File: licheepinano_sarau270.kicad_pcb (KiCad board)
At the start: 2 copper layers, 81.3 x 51.9 mm, 111 parts, among them Con1 SIM8050-6-0-14-01-A, Con2 >VALUE, Con3 USB_C_Wurth_632723130112, P1 RF2-03E-T-00-50-G, Q1 BC847B, Q2 BC847B, T1 FDN304P, U1 LAN9514I, U2 IP4220CZ6, U3 LILY-W132, U4 MAX-M8C, U5 TXB0104, X1 ABM3-25.000MHZ-D2Y-T

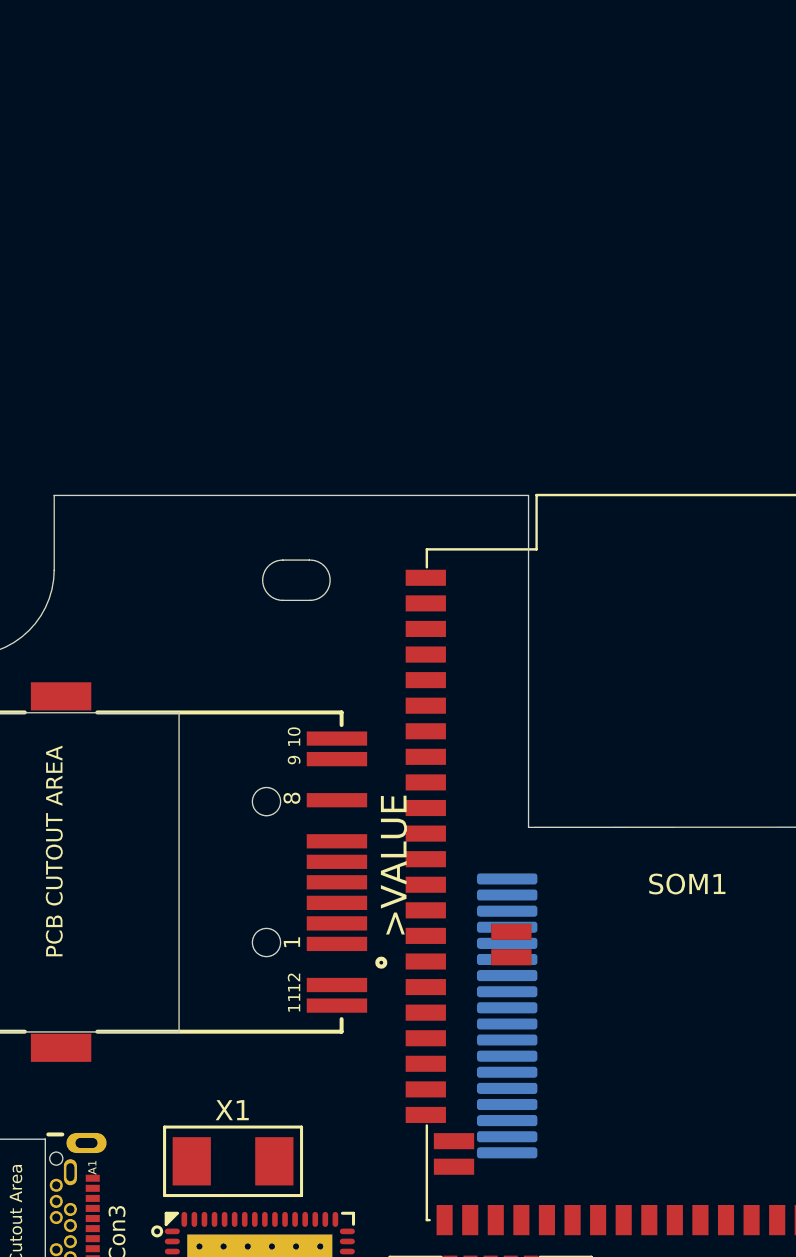
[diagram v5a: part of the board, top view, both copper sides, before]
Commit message: Schematic finished, with check ERC
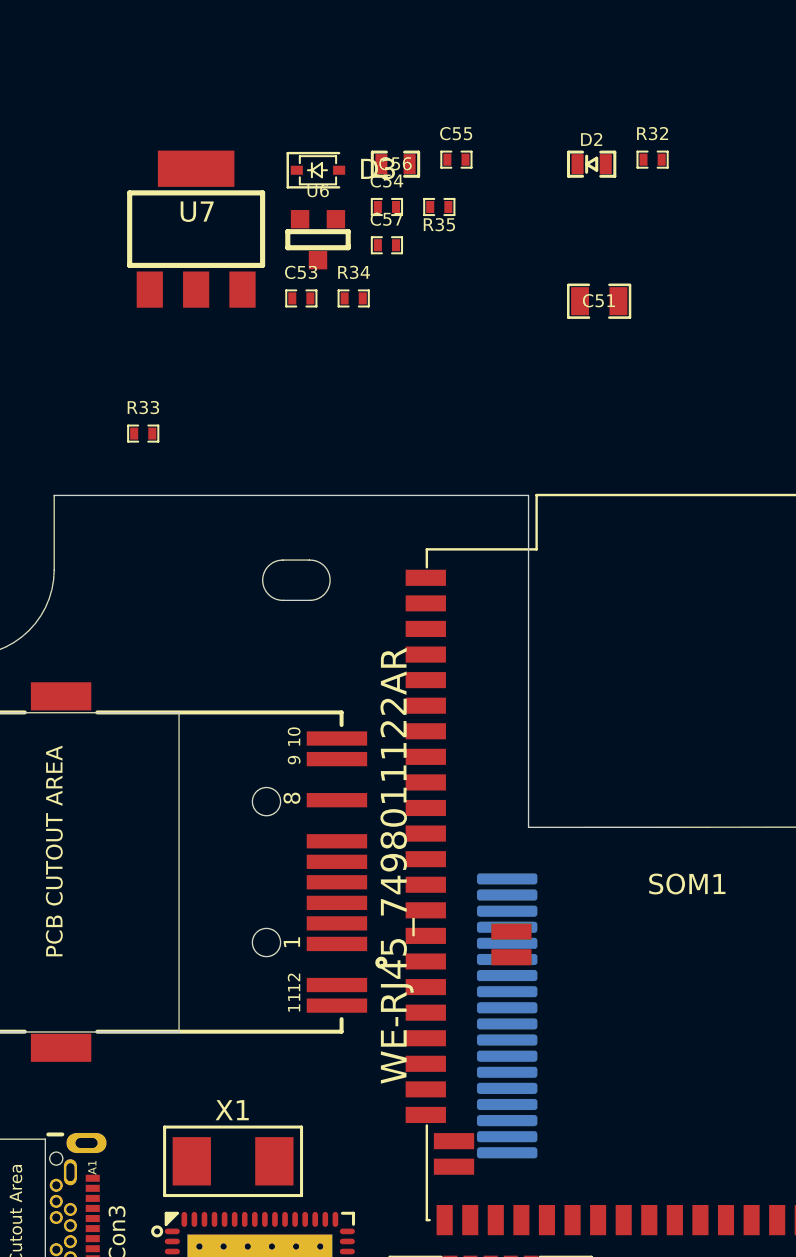
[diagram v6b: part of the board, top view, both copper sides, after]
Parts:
- added C51: 10uF/16V, Capacitors_Smd_0805:10uF_0805, F.Cu at (134.1, 62.8)
- added C53: 1uF/10V, Capacitors_Smd_0402:1uF_0402, F.Cu at (119.3, 62.7)
- added C54: 1uF/10V, Capacitors_Smd_0402:1uF_0402, F.Cu at (123.5, 58.1)
- added C55: 1uF/10V, Capacitors_Smd_0402:1uF_0402, F.Cu at (127.0, 55.8)
- added C56: 10uF/10V, Capacitors_Smd_0603:10uF_10V_0603, F.Cu at (123.9, 56.0)
- added C57: 1uF/10V, Capacitors_Smd_0402:1uF_0402, F.Cu at (123.5, 60.0)
- added D2: KPG-1608SURKC-T, Diodes:LED_KPG-1608SURKC-T, F.Cu at (133.7, 56.0)
- added D3: NSR0530H-D, Diodes:NSR0530H-D_SOD323, F.Cu at (120.1, 56.3)
- added R32: 470R, Resistor_Smd_0402:470R_0402, F.Cu at (136.7, 55.8)
- added R33: 47k, Resistor_Smd_0402:47k_0402, F.Cu at (111.4, 69.4)
- added R34: 1k5, Resistor_Smd_0402:1k5_0402, F.Cu at (121.9, 62.7)
- added R35: 3k3, Resistor_Smd_0402:3k3_0402, F.Cu at (126.1, 58.1)
- added U6: AP2127K-2.8TRG1, Linear:AP2127K-2.8TRG1_SOT23, F.Cu at (120.1, 59.8)
- added U7: LM317DCYR, Linear:LM317DCYR_SOT223, F.Cu at (114.0, 59.2)
- Con2: value >VALUE -> WE-RJ45_7498011122AR
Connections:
- net 3V8 renamed /Modem 3G/MODEM_POWER_IN
- C14 pad 1: /USB Hub Module/~HUB_RESET -> /LicheePi Nano SOM/GPIO_PD11
- C28 pad 1: /Modem 3G/LOCAL_MODEM_1V8_~RESET -> /LicheePi Nano SOM/GPIO_PD1
- C39 pad 1: /Logic Voltage Shifter/POWER_IN_HIGH_SIDE -> 3V3
- C40 pad 1: /Logic Voltage Shifter/POWER_IN_HIGH_SIDE -> 3V3
- C41 pad 1: /Logic Voltage Shifter/POWER_IN_LOW_SIDE -> /GPS Module/POWER_IN_1V8
- C42 pad 1: /Logic Voltage Shifter/POWER_IN_LOW_SIDE -> /GPS Module/POWER_IN_1V8
- Con3 pad A5: /Power Supply Module/USB_ID -> /LicheePi Nano SOM/USB_ID
- Con3 pad B5: /Power Supply Module/USB_ID -> /LicheePi Nano SOM/USB_ID
- DIS1 pad 1: /LCD Module/POWER_IN_GND -> GND
- DIS1 pad 2: (no net) -> /LicheePi Nano SOM/GPIO_PD19
- DIS1 pad 4: (no net) -> /LCD Module/DC
- DIS1 pad 8: /LCD Module/POWER_IN_GND -> GND
- DIS1 pad 9: (no net) -> /LCD Module/POWER_IN_2V8
- Modem1 pad 15: /Modem 3G/MODEM_PWR_ON -> /LicheePi Nano SOM/GPIO_PD0
- Modem1 pad 18: /Modem 3G/LOCAL_MODEM_1V8_~RESET -> /LicheePi Nano SOM/GPIO_PD1
- R13 pad 2: /Modem 3G/MODEM_PWR_ON -> /LicheePi Nano SOM/GPIO_PD0
- SOM1 pad 1: /LCD Module/MISO -> (no net)
- SOM1 pad 10: /Logic Voltage Shifter/SIG1_HIGH_PART -> /LCD Module/CS
- SOM1 pad 11: /Logic Voltage Shifter/SIG3_HIGH_PART -> (no net)
- SOM1 pad 12: /Logic Voltage Shifter/SIG2_HIGH_PART -> /LCD Module/MISO
- SOM1 pad 14: (no net) -> /LCD Module/CLK
- SOM1 pad 15: /Logic Voltage Shifter/SIG4_HIGH_PART -> (no net)
- SOM1 pad 16: (no net) -> /LCD Module/MOSI
- SOM1 pad 21: (no net) -> /LicheePi Nano SOM/GPIO_PD19
- SOM1 pad 22: (no net) -> Net-(D2-Pad2)
- SOM1 pad 25: (no net) -> /LicheePi Nano SOM/GPIO_PD5
- SOM1 pad 26: (no net) -> /Logic Voltage Shifter/SIG3_HIGH_PART
- SOM1 pad 27: (no net) -> /Logic Voltage Shifter/SIG4_HIGH_PART
- SOM1 pad 29: (no net) -> /LicheePi Nano SOM/GPIO_PD1
- SOM1 pad 3: /LCD Module/MOSI -> (no net)
- SOM1 pad 30: (no net) -> /LicheePi Nano SOM/GPIO_PD0
- SOM1 pad 31: (no net) -> /LicheePi Nano SOM/GPIO_PD11
- SOM1 pad 32: (no net) -> /UBlox WiFi Lily W132/ENABLE
- SOM1 pad 33: (no net) -> /LicheePi Nano SOM/GPIO_PD9
- SOM1 pad 34: (no net) -> /LCD Module/DC
- SOM1 pad 40: (no net) -> /Logic Voltage Shifter/SIG2_HIGH_PART
- SOM1 pad 41: (no net) -> /Logic Voltage Shifter/SIG1_HIGH_PART
- SOM1 pad 5: /LCD Module/CS -> (no net)
- SOM1 pad 63: (no net) -> /LicheePi Nano SOM/USB_ID
- SOM1 pad 7: /LCD Module/CLK -> (no net)
- U1 pad 12: /USB Hub Module/~HUB_RESET -> /LicheePi Nano SOM/GPIO_PD11
- U3 pad 14: (no net) -> /UBlox WiFi Lily W132/ENABLE
- U4 pad 9: (no net) -> /LicheePi Nano SOM/GPIO_PD9
- U5 pad 1: /Logic Voltage Shifter/POWER_IN_HIGH_SIDE -> 3V3
- U5 pad 14: /Logic Voltage Shifter/POWER_IN_LOW_SIDE -> /GPS Module/POWER_IN_1V8
- U5 pad 8: (no net) -> /LicheePi Nano SOM/GPIO_PD5

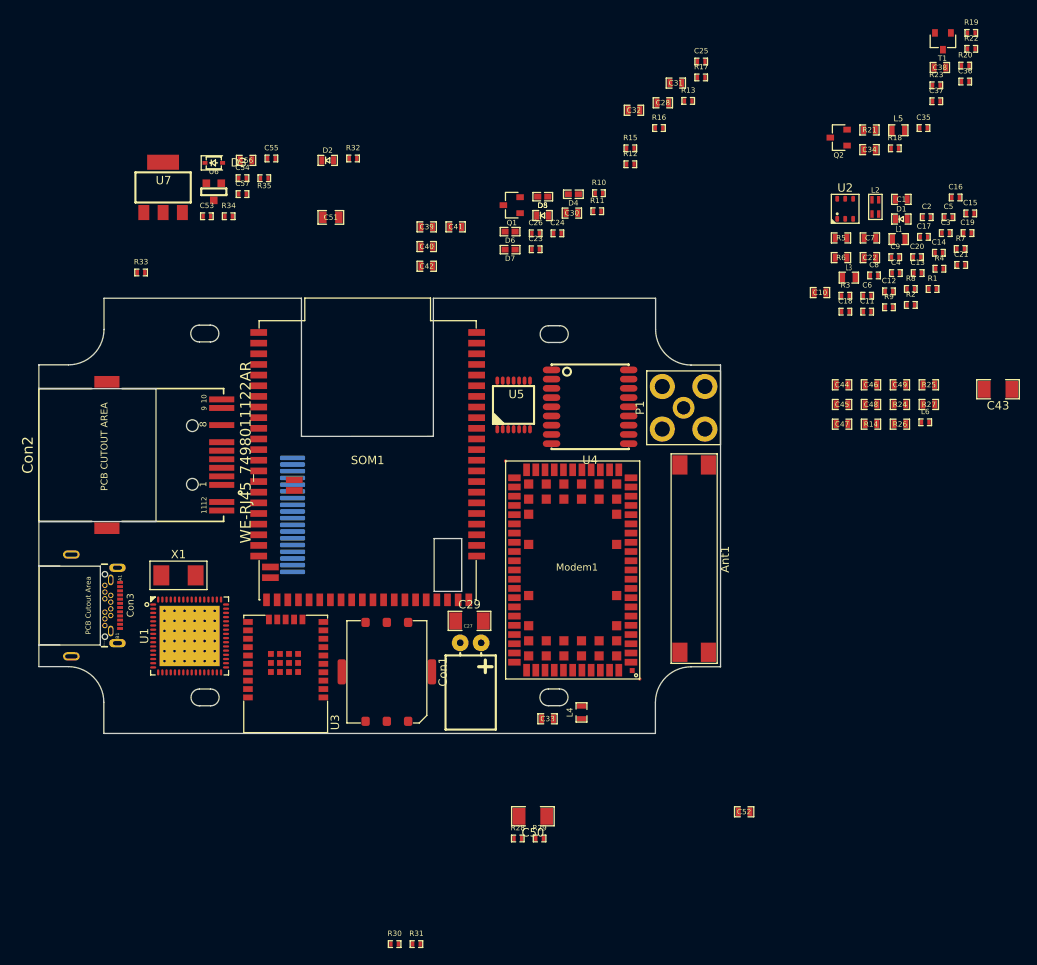
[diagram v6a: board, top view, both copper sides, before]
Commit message: Updated README.md and figurated components on pcb
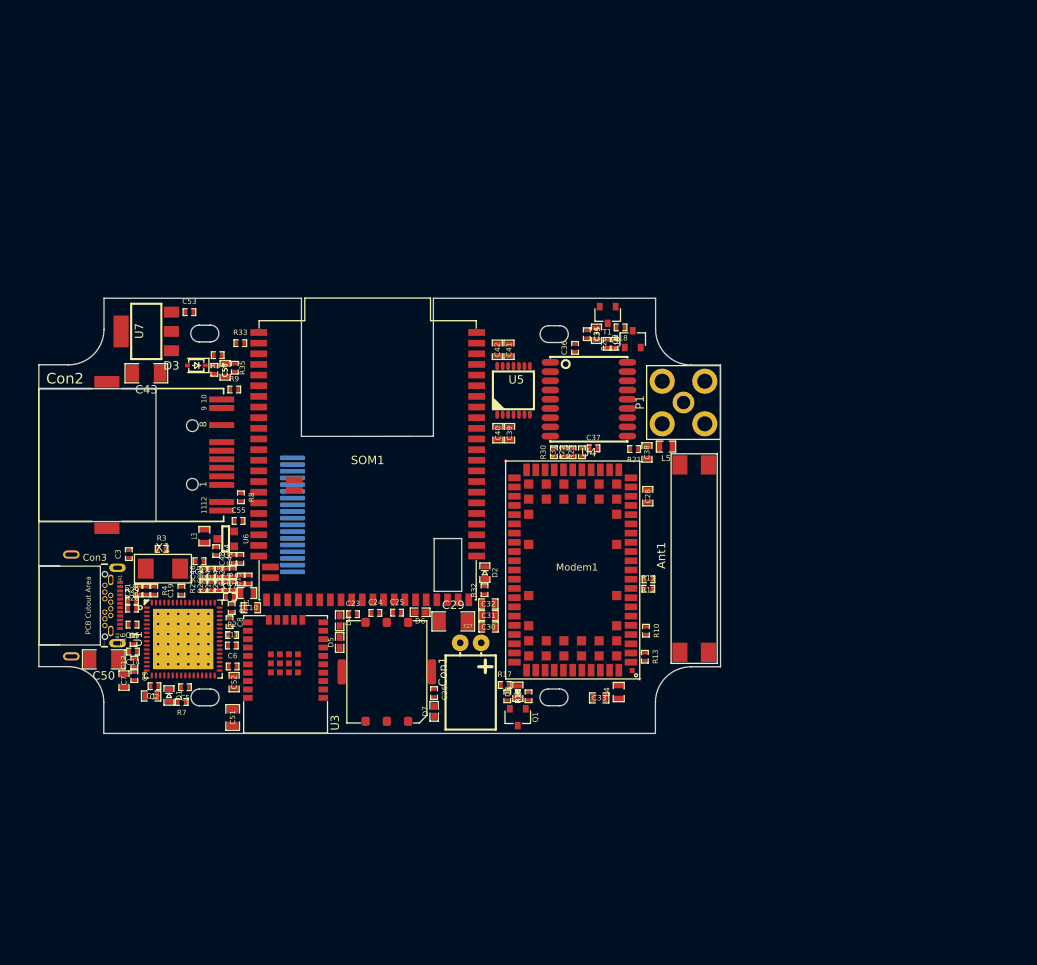
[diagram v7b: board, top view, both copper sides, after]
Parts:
- removed C22: 100nF/50V, Capacitors_Smd_0603:100nF_0603
- removed L2: DLW21HN900SQ2L, Inductors:DLW21HN900SQ2L
- removed R5, R6: 0R, Resistor_Smd_0603:0R_0603
- removed U2: IP4220CZ6, ESD_Protectors:IP4220CZ6_SOT457
- C44, C45, C46, C47: footprint Capacitors_Smd_0603:15pF_0603 -> Capacitors_Smd_0402:15pF_0402
- C48, C49: value 22nF/50V -> 22nF/25V; footprint Capacitors_Smd_0603:22nF_0603 -> Capacitors_Smd_0402:22nF_0402
- Con2: value WE-RJ45_7498011122AR -> >VALUE
- R14, R24, R25, R26: value 49R9 -> 49R9/1%; footprint Resistor_Smd_0603:49R9_0603 -> Resistor_Smd_0402:49R9_0402
- R21, R27: value 10R/1% -> 10R; footprint Resistor_Smd_0603:10R_0603 -> Resistor_Smd_0402:10R_0402
- moved C16 111.4 mm to (110.5, 113.2), turned to 90 degrees
- moved C15 111.3 mm to (110.4, 111.4), turned to 180 degrees
- moved C2 107.8 mm to (113.0, 118.7), turned to 180 degrees
- moved R7 107.5 mm to (116.3, 120.6), turned to 180 degrees
- moved C1 107.3 mm to (112.6, 119.9), turned to 180 degrees
- moved C14 107.3 mm to (110.5, 114.6), turned to 180 degrees
- moved C5 107.0 mm to (116.7, 118.8), turned to 180 degrees
- moved C21 105.6 mm to (111.1, 107.3), turned to 90 degrees
- moved C3 104.7 mm to (110.0, 103.0), turned to 90 degrees
- moved D1 104.2 mm to (114.8, 119.8), turned to 270 degrees
- moved C9 103.6 mm to (110.6, 117.5), turned to 270 degrees
- moved C7 103.5 mm to (109.4, 118.1), turned to 270 degrees
- moved C19 103.0 mm to (116.2, 107.3), turned to 90 degrees
- moved C43 101.6 mm to (112.0, 81.4)
- moved R4 101.2 mm to (113.0, 107.3), turned to 270 degrees
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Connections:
- C49 pad 1: GND -> Net-(C48-Pad1)
- C49 pad 2: Net-(C48-Pad1) -> GND
- L1 pad 2: (no net) -> Net-(C10-Pad1)
- Modem1 pad 17: VBUS -> (no net)
- U1 pad 1: /USB Hub Module/USB_HUB_5- -> /USB Hub Module/USB_D2_OUT_N
- U1 pad 2: /USB Hub Module/USB_HUB_5+ -> /USB Hub Module/USB_D2_OUT_P

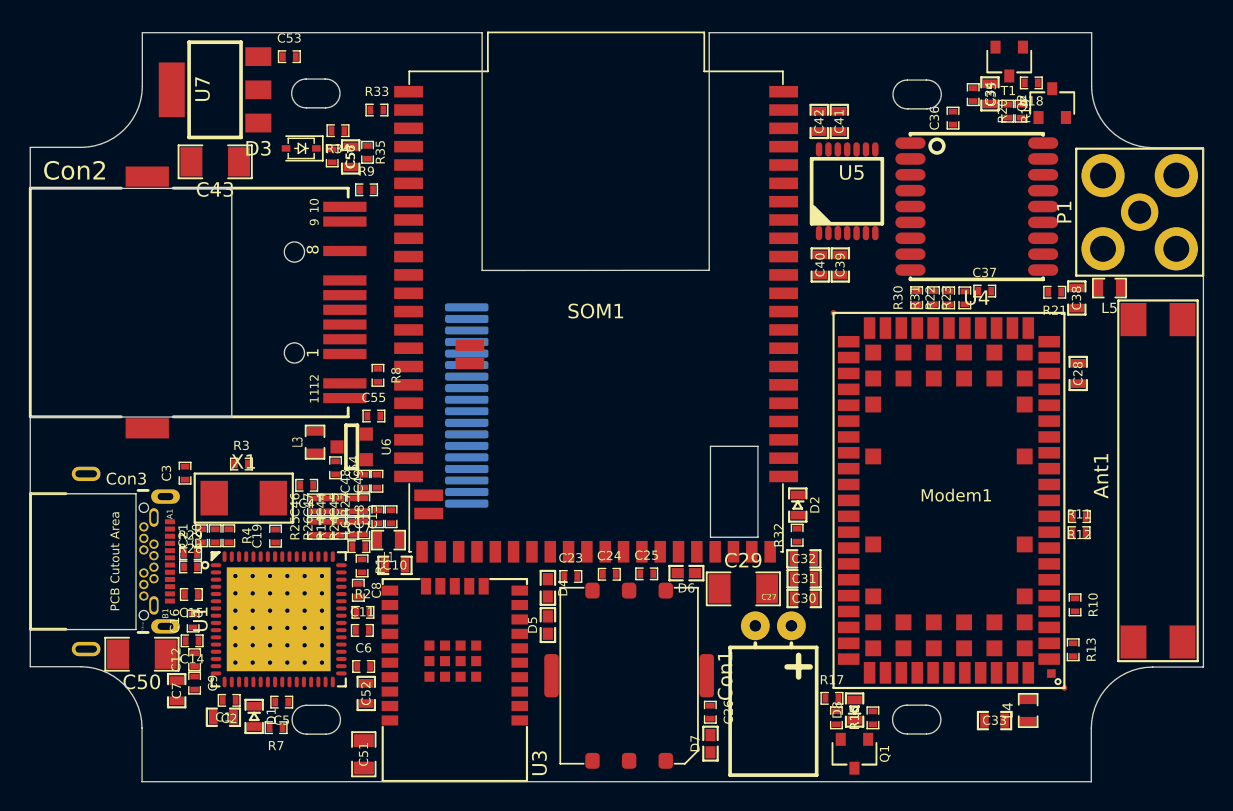
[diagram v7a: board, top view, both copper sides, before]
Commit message: Added most of the pcb connections
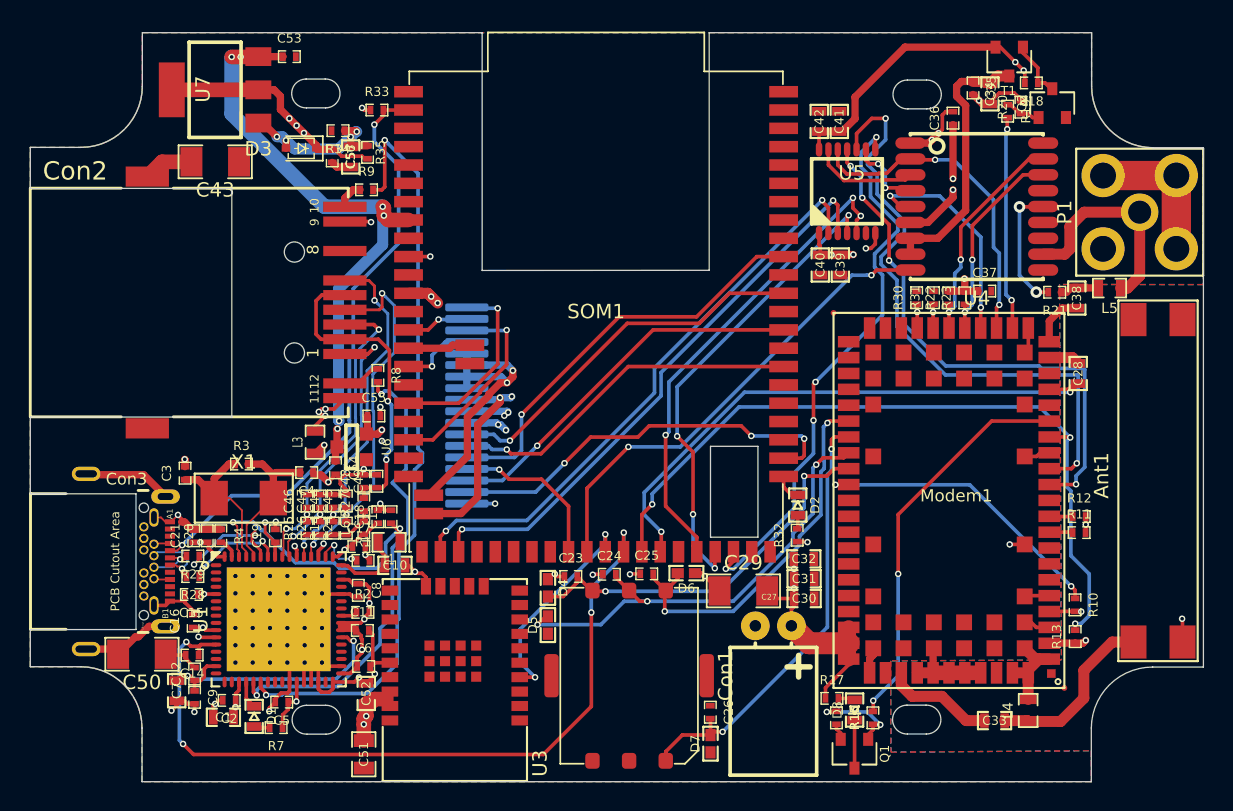
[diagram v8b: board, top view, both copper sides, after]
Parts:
- moved C12 0.99 mm to (110.6, 116.9)
- moved C14 0.99 mm to (110.5, 115.6)
- moved C9 0.99 mm to (110.6, 118.5)
- moved R13 0.92 mm to (171.7, 114.3), turned to 90 degrees
- moved C4 0.88 mm to (118.4, 102.9)
- moved R28 0.69 mm to (110.5, 110.2), turned to 180 degrees
- moved C20 0.55 mm to (111.5, 107.3)
- moved C21 0.55 mm to (110.6, 107.3)
- moved R4 0.55 mm to (112.4, 107.3)
- moved C44 0.52 mm to (120.2, 104.9)
- moved C45 0.52 mm to (121.1, 104.9)
- moved C46 0.52 mm to (118.4, 104.9)
- moved C47 0.52 mm to (119.3, 104.9)
- moved C35 0.46 mm to (164.6, 76.3)
- moved R14 0.45 mm to (120.2, 106.8)
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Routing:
- net GND: track 0.00 -> 203.3 mm, vias 0 -> 30
- net /Modem 3G/MODEM_POWER_IN: track 0.00 -> 93.8 mm, vias 0 -> 5
- net /LicheePi Nano SOM/POWER_IN_5V0: track 0.00 -> 70.8 mm, vias 0 -> 6
- net /GPS Module/POWER_IN_1V8: track 0.00 -> 62.7 mm, vias 0 -> 3
- net /LicheePi Nano SOM/GPIO_PD11: track 0.00 -> 54.5 mm, vias 0 -> 4
- net 3V3: track 0.00 -> 53.4 mm, vias 0 -> 18
- net Net-(R9-Pad2): track 0.00 -> 53.3 mm, vias 0 -> 2
- net /LicheePi Nano SOM/GPIO_PD0: track 0.00 -> 52.9 mm, vias 0 -> 3
- net /GPS Module/GPS_V_BCKP: track 0.00 -> 47.1 mm, vias 0 -> 3
- net /Ethernet Connector Module/POWER_IN_3V3: track 0.00 -> 43.4 mm, vias 0 -> 8
- net /Logic Voltage Shifter/SIG4_LOW_PART: track 0.00 -> 42.8 mm, vias 0 -> 2
- net /LicheePi Nano SOM/USB_ID: track 0.00 -> 42.3 mm, vias 0 -> 2
- net /Logic Voltage Shifter/SIG1_HIGH_PART: track 0.00 -> 40.7 mm, vias 0 -> 2
- net /Logic Voltage Shifter/SIG2_HIGH_PART: track 0.00 -> 40.2 mm, vias 0 -> 2
- net /LicheePi Nano SOM/GPIO_PD1: track 0.00 -> 40.0 mm, vias 0 -> 2
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- added copper zone on In1.Cu, net 3V3
- added copper zone on B.Cu, net GND
- added copper zone on F.Cu, net GND
- added copper zone on In2.Cu, net GND
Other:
- copper layers 2 -> 4
- net class Default: trace_width 0.25 -> 0.254; via_dia 0.8 -> 0.45; via_drill 0.4 -> 0.25
- rule pad_to_mask_clearance: 0 -> 0.05
- rule trace_min: 0.2 -> 0.1
- rule via_min_drill: 0.3 -> 0.2
- rule via_min_size: 0.4 -> 0.2
